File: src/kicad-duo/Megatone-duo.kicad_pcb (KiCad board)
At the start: 2 copper layers, 28.4 x 28.4 mm, 22 parts, among them P1 Classic, P2 Boost, P3 Gnd, SW1 LORLIN_2X6

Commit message: 2014-10-23
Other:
- board text added: "megatone DUO"
- board text removed: "megatone DUO v6"

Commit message: 2014-10-23 - updated solo and duo pcbs
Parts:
- moved P2 0.51 mm to (175.3, 68.1)
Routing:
- net Net-(P2-Pad1): track 11.1 -> 11.6 mm
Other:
- board size 28.4 x 28.4 mm -> 27.4 x 28.4 mm

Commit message: update pcbs and generate fab plots
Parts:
- moved P1 0.52 mm to (168.4, 70.1), turned to 30 degrees
- turned P3 to 330 degrees

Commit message: minor pcb mods
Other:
- board text added: "Open Hardware"

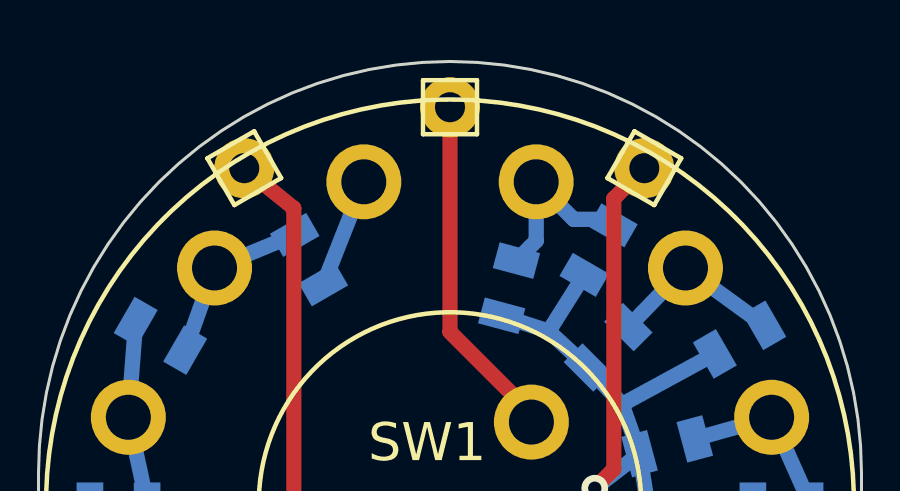
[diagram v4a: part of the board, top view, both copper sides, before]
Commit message: moving output pins
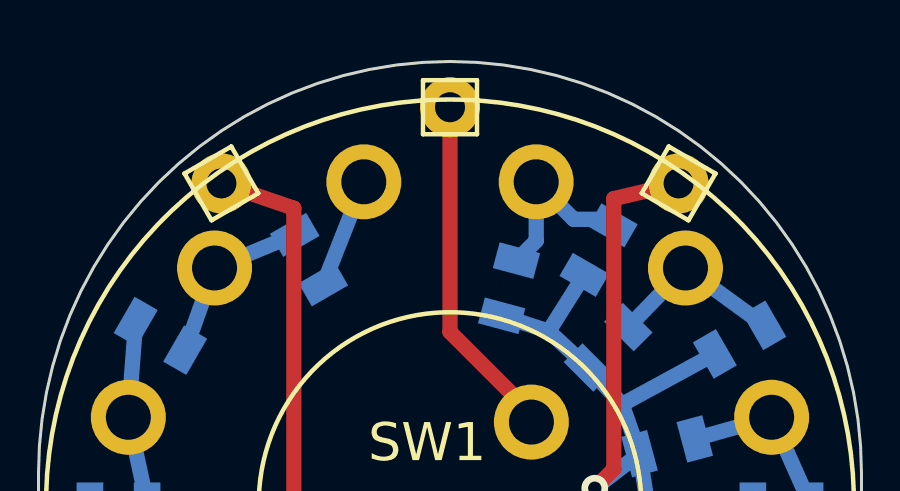
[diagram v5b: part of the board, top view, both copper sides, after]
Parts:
- moved P3 1.25 mm to (182.9, 70.6)
- moved P1 0.92 mm to (167.6, 70.6)
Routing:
- net GND: track 53.5 -> 54.3 mm
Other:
- board text added: "v 6.1"
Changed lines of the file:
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@@
-(kicad_pcb (version 4) (host pcbnew "(2014-10-31 BZR 5247)-product")
+(kicad_pcb (version 4) (host pcbnew "(2014-12-07 BZR 5316)-product")
   (general
     (links 38)
     (no_connects 0)
-    (area 161.493999 66.497999 189.026001 95.046001)
+    (area 161.340181 65.206 189.179819 95.199819)
     (thickness 1.6)
-    (drawings 12)
+    (drawings 13)
     (tracks 62)
     (zones 0)
@@
   )
   (module Connect:SIL-1 (layer F.Cu)
-    (at 168.402 70.104 30)
+    (at 167.64 70.612 30)
     (descr "Connecteurs 1 pin")
     (tags "CONN DEV")
@@
   )
   (module Connect:SIL-1 (layer F.Cu)
-    (at 181.737 70.104 330)
+    (at 182.88 70.612 330)
     (descr "Connecteurs 1 pin")
     (tags "CONN DEV")
@@
       (net 10 "Net-(P2-Pad1)"))
   )
+  (gr_text "v 6.1" (at 170.434 81.026 315) (layer B.SilkS)
+    (effects (font (size 0.762 0.762) (thickness 0.1905)) (justify mirror))
+  )
   (gr_text "Open Hardware" (at 174.498 82.042 315) (layer B.SilkS)
     (effects (font (size 0.762 0.762) (thickness 0.1905)) (justify mirror))
@@
     (effects (font (size 0.762 0.762) (thickness 0.1905)) (justify mirror))
   )
-  (gr_text classic (at 171.196 68.072 20) (layer B.SilkS)
+  (gr_text classic (at 170.688 68.58 20) (layer B.SilkS)
     (effects (font (size 0.889 0.889) (thickness 0.22225)) (justify mirror))
   )
@@
     (effects (font (size 0.889 0.889) (thickness 0.22225)) (justify mirror))
   )
-  (gr_text gnd (at 184.15 70.866 320) (layer B.SilkS)
+  (gr_text gnd (at 185.166 71.628 320) (layer B.SilkS)
     (effects (font (size 0.889 0.889) (thickness 0.22225)) (justify mirror))
   )
@@
   (segment (start 180.086 80.772) (end 180.721 80.137) (width 0.508) (layer F.Cu) (net 2))
   (segment (start 180.721 80.137) (end 180.721 71.12) (width 0.508) (layer F.Cu) (net 2))
-  (segment (start 180.721 71.12) (end 181.737 70.104) (width 0.508) (layer F.Cu) (net 2))
+  (segment (start 180.721 71.12) (end 182.88 70.612) (width 0.508) (layer F.Cu) (net 2) (status 20))
   (segment (start 181.578956 79.621525) (end 180.086 80.772) (width 0.508) (layer B.Cu) (net 2))
   (via (at 180.086 80.772) (size 0.889) (layers F.Cu B.Cu) (net 2))
@@
   (segment (start 172.55 83.98) (end 170.053 81.483) (width 0.508) (layer F.Cu) (net 9))
   (segment (start 170.053 81.483) (end 170.053 71.4375) (width 0.508) (layer F.Cu) (net 9))
-  (segment (start 170.053 71.4375) (end 168.402 70.104) (width 0.508) (layer F.Cu) (net 9) (status 20))
+  (segment (start 170.053 71.4375) (end 167.64 70.612) (width 0.508) (layer F.Cu) (net 9) (status 20))
   (segment (start 177.97272 78.56728) (end 177.97272 78.27772) (width 0.508) (layer F.Cu) (net 10))
   (segment (start 177.97272 78.27772) (end 175.26 75.565) (width 0.508) (layer F.Cu) (net 10))

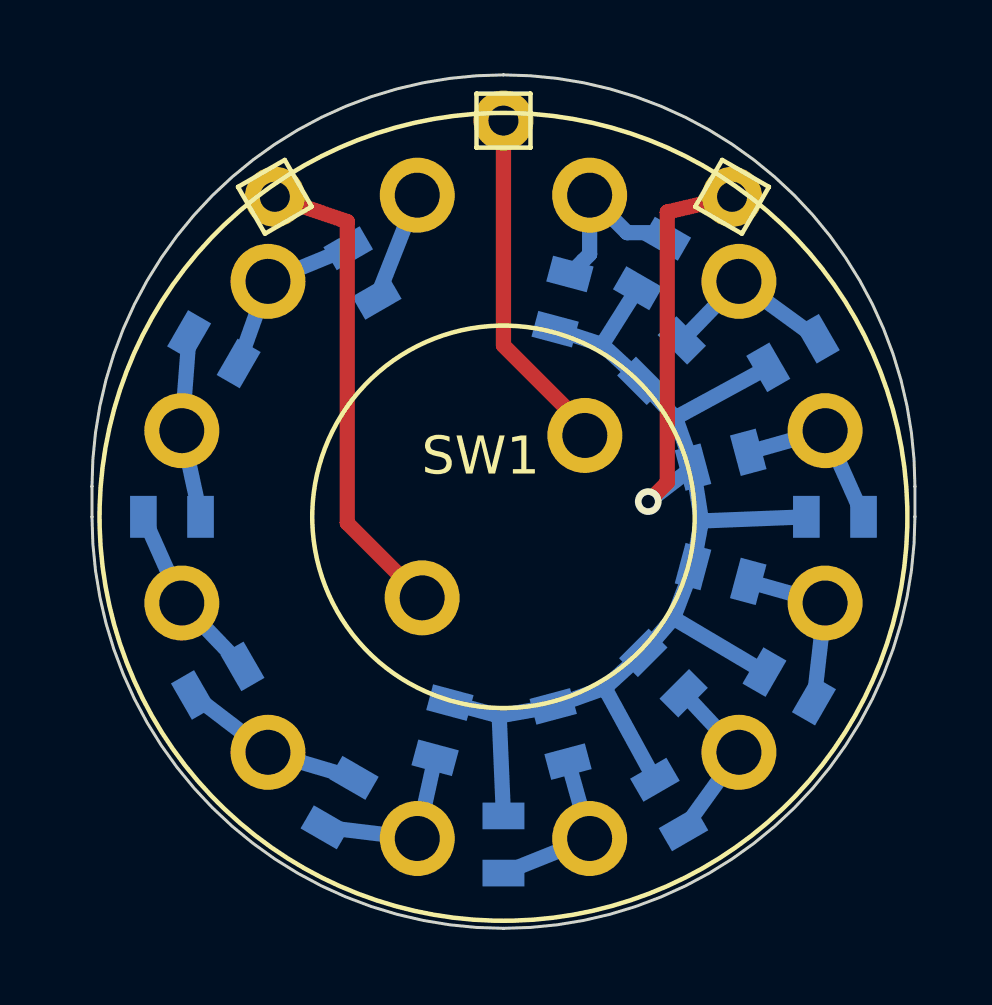
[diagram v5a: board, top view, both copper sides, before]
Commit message: Turning output pins by 90°
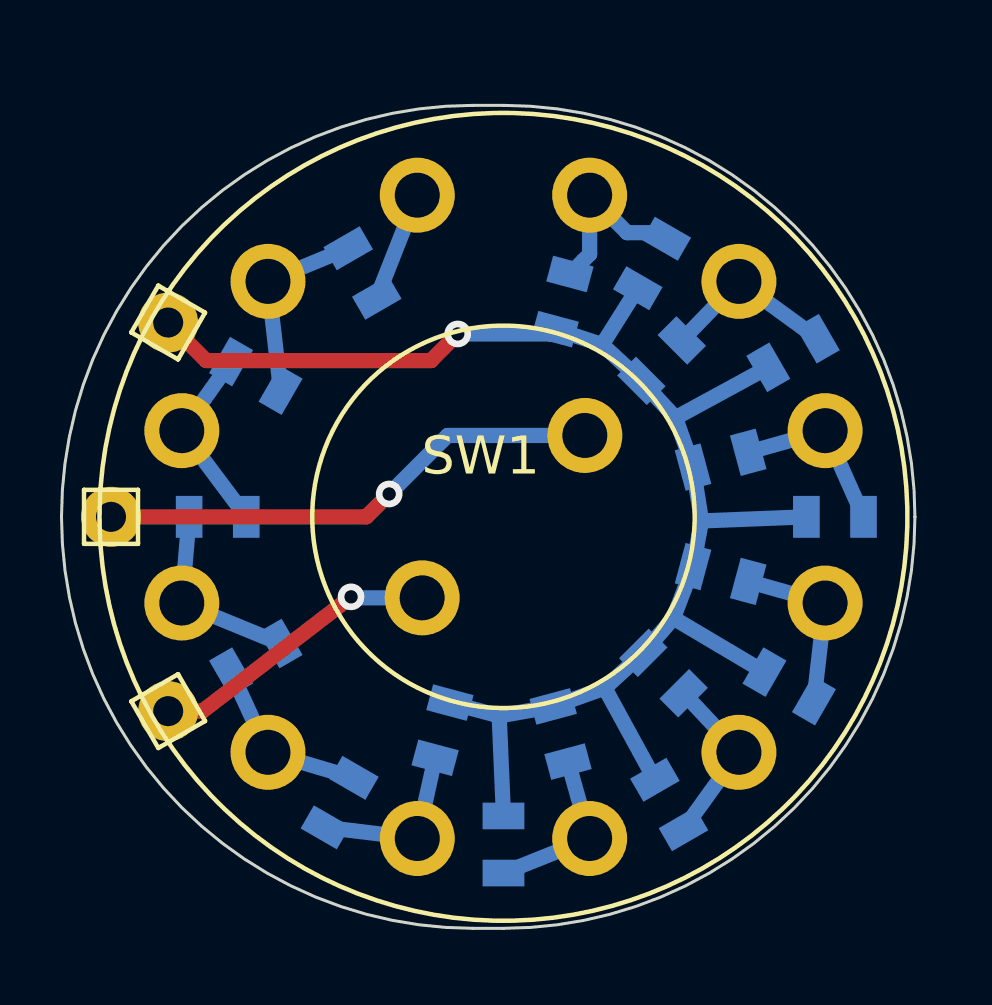
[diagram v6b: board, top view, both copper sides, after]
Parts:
- R10: value 100K -> 47K
- R7: value 10K -> 5K
- R8: value 22K -> 10K
- R9: value 47K -> 22K
- moved P3 19.3 mm to (164.1, 74.8)
- moved P2 18.6 mm to (162.2, 81.3)
- moved P1 17.5 mm to (164.1, 87.8)
- moved R10 1.66 mm to (167.0, 76.6)
- moved R9 1.52 mm to (165.7, 81.3)
- moved R8 1.48 mm to (167.0, 86.0)
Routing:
- net Net-(P1-Pad1): track 16.1 -> 9.78 mm, vias 0 -> 1
- net Net-(P2-Pad1): track 11.6 -> 17.2 mm, vias 0 -> 1
- net Net-(R10-Pad2): track 5.80 -> 6.54 mm
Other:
- board size 27.4 x 28.4 mm -> 28.4 x 27.4 mm
- board text added: "megatone DUO 6.2"
- board text removed: "megatone DUO"

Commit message: plots for v6.2
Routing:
- net Net-(P2-Pad1): track 17.2 -> 16.9 mm, vias 1 -> 0
- net Net-(P1-Pad1): track 9.78 -> 10.0 mm, vias 1 -> 0
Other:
- board text added: "Megatone DUO 6.2"
- board text removed: "megatone DUO 6.2"
- board text removed: "v 6.1"
